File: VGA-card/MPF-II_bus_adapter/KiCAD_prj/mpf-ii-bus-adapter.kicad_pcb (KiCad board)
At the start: 2 copper layers, 100 x 34.4 mm, 33 parts, among them J1 Bus_Apple_II_Card_Side, J10 USER1_Sel, J11 INH_Sel, J12 RDY_Sel, J13 COLREF_Sel, J14 IOSTRB_Sel, J15 Q3_Sel, J16 Pin, J17 Pin, J18 Pin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

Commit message: PCB updated
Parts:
- moved J26 26.0 mm to (150.0, 103.2)
- moved J6 4.25 mm to (154.5, 100.7)
- moved J12 4.10 mm to (180.6, 100.7)
- moved J14 4.00 mm to (159.5, 103.2)
- moved J7 3.85 mm to (175.1, 100.7)
- moved J9 3.85 mm to (164.6, 100.7)
- moved J11 3.80 mm to (169.8, 100.7)
- moved J8 3.75 mm to (185.5, 100.7)
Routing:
- net GND: track 0.00 -> 114.4 mm
- net +5V: track 0.00 -> 87.4 mm
- net Net-(J3-Pin_1): track 0.00 -> 7.42 mm
- net Net-(J23-Pin_1): track 0.00 -> 3.71 mm
- net Net-(J24-Pin_1): track 0.00 -> 3.65 mm
- net Net-(J18-Pin_1): track 0.00 -> 3.52 mm
- net Net-(J17-Pin_1): track 0.00 -> 3.46 mm
- net Net-(J22-Pin_1): track 0.00 -> 3.33 mm
- net Net-(J25-Pin_1): track 0.00 -> 3.27 mm
- net Net-(J20-Pin_1): track 0.00 -> 3.24 mm
- net Net-(J16-Pin_1): track 0.00 -> 3.18 mm
- net Net-(J19-Pin_1): track 0.00 -> 3.14 mm
- net Net-(J21-Pin_1): track 0.00 -> 3.05 mm
- net /Q3: track 0.00 -> 0.91 mm
- net /A_PHI0: track 0.00 -> 0.83 mm
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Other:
- board size 100 x 34.4 mm -> 99.2 x 34.4 mm

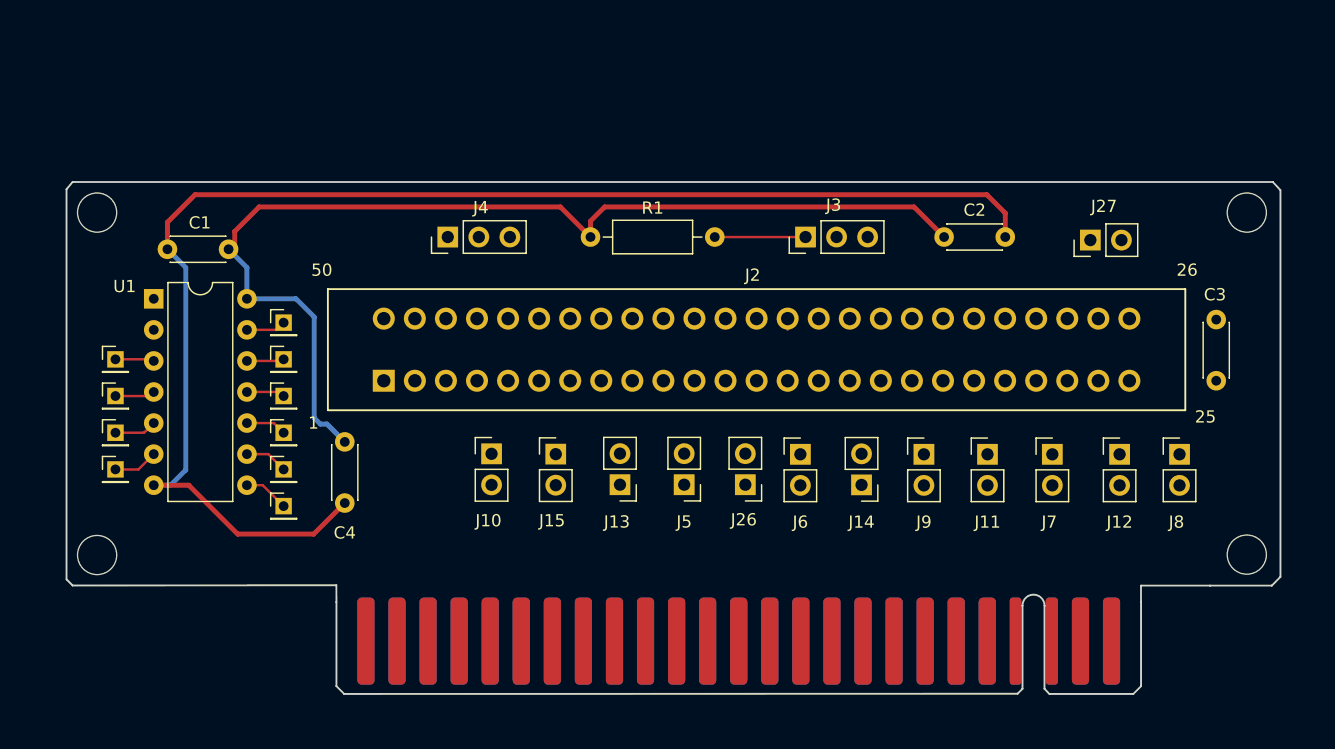
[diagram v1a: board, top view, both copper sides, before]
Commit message: PCB edge cut updated
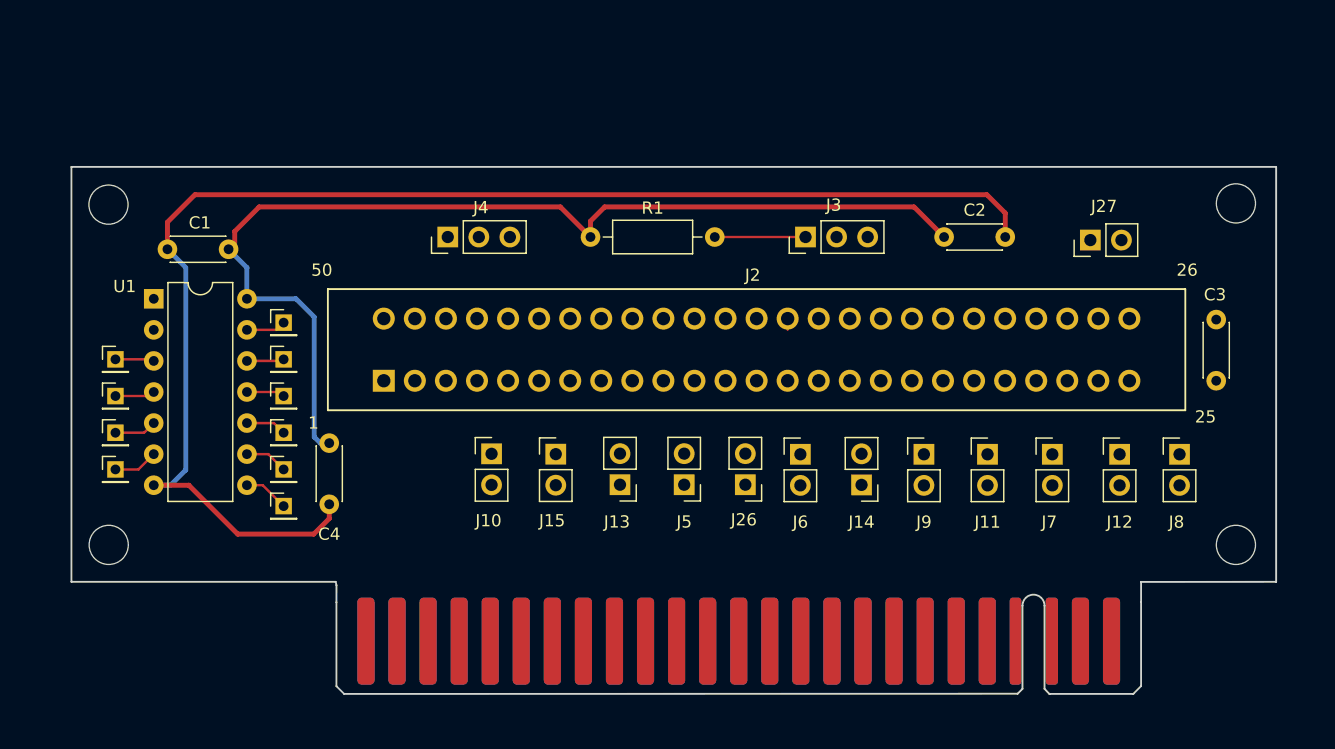
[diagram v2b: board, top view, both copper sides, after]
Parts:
- moved C4 1.27 mm to (116.0, 99.8)
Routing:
- net GND: track 114.4 -> 113.7 mm
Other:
- board size 99.2 x 34.4 mm -> 98.5 x 35.6 mm
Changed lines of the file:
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@@
 	(footprint "Capacitor_THT:C_Disc_D4.3mm_W1.9mm_P5.00mm"
 		(layer "F.Cu")
-		(at 117.25 99.71 -90)
+		(at 115.98 99.81 -90)
 		(descr "C, Disc series, Radial, pin pitch=5.00mm, , diameter*width=4.3*1.9mm^2, Capacitor, http://www.vishay.com/docs/45233/krseries.pdf")
 		(tags "C Disc series Radial pin pitch 5.00mm  diameter 4.3mm width 1.9mm Capacitor")
@@
 		)
 	)
-	(gr_circle
-		(center 97 80.96)
-		(end 98.25 81.96)
+	(gr_line
+		(start 193.4 77.225)
+		(end 193.4 111.15)
 		(stroke
-			(width 0.05)
+			(width 0.15)
 			(type default)
 		)
-		(fill none)
 		(layer "Edge.Cuts")
 	)
 	(gr_line
-		(start 193.05 111.46)
-		(end 188 111.46)
+		(start 94.9 77.225)
+		(end 193.4 77.225)
 		(stroke
 			(width 0.15)
@@
 	)
 	(gr_line
-		(start 193.05 111.46)
-		(end 193.75 110.745)
+		(start 116.5 111.15)
+		(end 94.9 111.15)
 		(stroke
 			(width 0.15)
@@
 		(layer "Edge.Cuts")
 	)
-	(gr_line
-		(start 193.75 110.75)
-		(end 193.75 79.125)
+	(gr_circle
+		(center 97.93 80.31)
+		(end 99.18 81.31)
 		(stroke
-			(width 0.15)
+			(width 0.05)
 			(type default)
 		)
+		(fill none)
 		(layer "Edge.Cuts")
 	)
 	(gr_line
-		(start 94.5 110.95)
-		(end 94.5 79.05)
+		(start 94.9 111.15)
+		(end 94.9 77.225)
 		(stroke
 			(width 0.15)
@@
 	)
 	(gr_line
-		(start 193.125 78.46)
-		(end 95 78.46)
+		(start 116.57 111.43)
+		(end 116.5 111.15)
 		(stroke
 			(width 0.15)
@@
 		(layer "Edge.Cuts")
 	)
-	(gr_line
-		(start 193.125002 78.454998)
-		(end 193.75 79.125)
+	(gr_circle
+		(center 97.95 108.13)
+		(end 96.7 109.13)
 		(stroke
-			(width 0.15)
+			(width 0.05)
 			(type default)
 		)
+		(fill none)
 		(layer "Edge.Cuts")
 	)
 	(gr_line
-		(start 95 78.46)
-		(end 94.5 79.05)
+		(start 193.4 111.15)
+		(end 182.35 111.16)
 		(stroke
 			(width 0.15)
@@
 	)
 	(gr_line
-		(start 95 111.45)
-		(end 94.5 110.95)
+		(start 182.353 112.825)
+		(end 182.35 111.16)
 		(stroke
 			(width 0.15)
@@
 	)
 	(gr_circle
-		(center 97 108.96)
-		(end 95.75 109.96)
+		(center 190.11 108.13)
+		(end 191.36 109.13)
 		(stroke
 			(width 0.05)
@@
 		(layer "Edge.Cuts")
 	)
-	(gr_line
-		(start 182.353 112.825)
-		(end 182.35 111.46)
-		(stroke
-			(width 0.15)
-			(type default)
-		)
-		(layer "Edge.Cuts")
-	)
 	(gr_circle
-		(center 191 108.925781)
-		(end 192.25 109.925781)
+		(center 190.11 80.21)
+		(end 191.36 79.21)
 		(stroke
 			(width 0.05)
@@
 	)
 	(gr_line
-		(start 116.56 111.43)
-		(end 95 111.45)
+		(start 116.567 112.825)
+		(end 116.57 111.43)
 		(stroke
 			(width 0.15)
@@
 		(layer "Edge.Cuts")
 	)
-	(gr_circle
-		(center 191 80.96)
-		(end 192.25 79.96)
+	(gr_rect
+		(start 94.9 77.225)
+		(end 193.4 111.15)
 		(stroke
-			(width 0.05)
+			(width 0.2)
 			(type default)
 		)
 		(fill none)
-		(layer "Edge.Cuts")
+		(layer "Margin")
 	)
 	(gr_line
-		(start 116.567 112.825)
-		(end 116.559988 111.43)
+		(start 116.61 111.44)
+		(end 116.43 111.16)
 		(stroke
-			(width 0.15)
-			(type default)
-		)
-		(layer "Edge.Cuts")
-	)
-	(gr_line
-		(start 188 111.46)
-		(end 182.35 111.46)
-		(stroke
-			(width 0.15)
+			(width 0.1)
 			(type default)
 		)
-		(layer "Edge.Cuts")
+		(layer "Margin")
 	)
 	(segment
@@
 	)
 	(segment
-		(start 114.75 97.75)
-		(end 115.25 98.25)
+		(start 114.75 99.31)
+		(end 115.25 99.81)
 		(width 0.4)
 		(layer "B.Cu")
@@
 	)
 	(segment
-		(start 115.25 98.25)
-		(end 115.79 98.25)
+		(start 115.25 99.81)
+		(end 115.98 99.81)
 		(width 0.4)
 		(layer "B.Cu")
@@
 	)
 	(segment
-		(start 109.25 85.46)
-		(end 107.75 83.96)
-		(width 0.4)
-		(layer "B.Cu")
-		(net 1)
-	)
-	(segment
 		(start 114.75 89.5)
-		(end 114.75 97.75)
+		(end 114.75 99.31)
 		(width 0.4)
 		(layer "B.Cu")
@@
 	)
 	(segment
-		(start 115.79 98.25)
-		(end 117.25 99.71)
+		(start 109.25 85.46)
+		(end 107.75 83.96)
 		(width 0.4)
 		(layer "B.Cu")
@@
 	)
 	(segment
+		(start 115.98 105.98)
+		(end 115.98 104.81)
+		(width 0.4)
+		(layer "F.Cu")
+		(net 2)
+	)
+	(segment
 		(start 171.25 81)
 		(end 171.25 82.96)
@@
 	)
 	(segment
-		(start 117.25 104.71)
-		(end 114.71 107.25)
+		(start 105 79.5)
+		(end 169.75 79.5)
 		(width 0.4)
 		(layer "F.Cu")
@@
 	)
 	(segment
-		(start 105 79.5)
-		(end 169.75 79.5)
+		(start 114.71 107.25)
+		(end 115.98 105.98)
 		(width 0.4)
 		(layer "F.Cu")

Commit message: PCB updated
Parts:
- added G***: LOGO, LOGO, F.Cu at (103.9, 107.7)
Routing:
- net /PHI1: track 0.00 -> 87.8 mm, vias 0 -> 1
- net +5V: track 87.1 -> 153.1 mm
- net /M_DEVSEL: track 0.00 -> 54.5 mm, vias 0 -> 2
- net /M_PHI2: track 0.00 -> 43.6 mm
- net Net-(J4-Pin_1): track 0.00 -> 35.2 mm
- net /D3: track 0.00 -> 31.2 mm
- net /D2: track 0.00 -> 30.1 mm
- net -5V: track 0.00 -> 29.8 mm
- net /2M: track 0.00 -> 29.1 mm, vias 0 -> 2
- net +12V: track 0.00 -> 28.9 mm
- net /D1: track 0.00 -> 28.8 mm
- net /D7: track 0.00 -> 28.7 mm
- net /D0: track 0.00 -> 28.3 mm
- net /D5: track 0.80 -> 28.9 mm
- net /EXT6: track 0.00 -> 28.0 mm, vias 0 -> 1
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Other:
- board text added: "MPF-II Bus Adapter, Rev A"

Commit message: PCB is ready
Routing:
- net GND: track 140.2 -> 173.7 mm
- net /RESET: track 0.00 -> 32.5 mm
- net /INTIN: track 0.00 -> 28.5 mm
- net /DMAIN: track 0.00 -> 27.4 mm
- net /M_IRQ: track 0.00 -> 25.4 mm, vias 0 -> 1
- net /A_IRQ: track 0.00 -> 24.9 mm
- net /M_RDY: track 0.00 -> 23.0 mm
- net /INTOUT: track 0.00 -> 22.9 mm, vias 0 -> 1
- net /DMAOUT: track 0.00 -> 21.9 mm, vias 0 -> 1
- net /EXTE: track 0.62 -> 18.3 mm, vias 0 -> 1
- net /A_NMI: track 0.00 -> 16.6 mm
- net /M_DMA: track 0.00 -> 16.3 mm
- net /M_NMI: track 0.00 -> 15.7 mm
- net /M_INH: track 0.00 -> 15.7 mm, vias 0 -> 1
- net /A_RDY: track 0.00 -> 14.2 mm
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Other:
- board text added: "mpf-ii_retro_6502 at Github"

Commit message: PCB updated
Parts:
- moved G*** 0.75 mm to (104.6, 107.6)
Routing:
- net +5V: track 153.1 -> 152.0 mm
- net GND: track 173.7 -> 172.5 mm
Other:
- outline, holes or cut-outs redrawn
- board text added: "mpf-ii_retro_6502 on GitHub"
- board text removed: "mpf-ii_retro_6502 at Github"
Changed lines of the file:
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@@
 	(footprint "LOGO"
 		(layer "F.Cu")
-		(at 103.9 107.725)
+		(at 104.648751 107.644678)
 		(property "Reference" "G***"
 			(at 0 0 0)
@@
 	)
 	(gr_circle
-		(center 97.93 80.31)
-		(end 99.18 81.31)
+		(center 98.09 80.320781)
+		(end 99.34 81.320781)
 		(stroke
 			(width 0.05)
@@
 	)
 	(gr_circle
-		(center 97.95 108.13)
-		(end 96.7 109.13)
+		(center 98.1 107.390781)
+		(end 96.85 108.390781)
 		(stroke
 			(width 0.05)
@@
 	)
 	(gr_circle
-		(center 190.11 108.13)
-		(end 191.36 109.13)
+		(center 190.225 107.425)
+		(end 191.475 108.425)
 		(stroke
 			(width 0.05)
@@
 	)
 	(gr_circle
-		(center 190.11 80.21)
-		(end 191.36 79.21)
+		(center 190.47 80.320781)
+		(end 191.72 79.320781)
 		(stroke
 			(width 0.05)
@@
 		(layer "Margin")
 	)
-	(gr_text "mpf-ii_retro_6502 at Github"
-		(at 164.15 78.75 0)
+	(gr_text "mpf-ii_retro_6502 on GitHub"
+		(at 159.42 78.77 0)
 		(layer "F.SilkS")
 		(effects
@@
 	)
 	(segment
-		(start 188.5 97.85)
-		(end 189.5 98.85)
-		(width 0.5)
-		(layer "F.Cu")
-		(net 1)
-	)
-	(segment
 		(start 108.25 82.5)
 		(end 108.25 83.46)
@@
 	)
 	(segment
-		(start 179.94 110.61)
-		(end 179.94 116)
+		(start 187.95 104.575)
+		(end 187.95 98.4)
 		(width 0.5)
 		(layer "F.Cu")
@@
 	)
 	(segment
-		(start 181.2 109.35)
+		(start 179.94 116)
 		(end 179.94 110.61)
 		(width 0.5)
@@
 	)
 	(segment
-		(start 189.5 98.85)
-		(end 189.5 104.05)
+		(start 186.2 105.25)
+		(end 187.275 105.25)
 		(width 0.5)
 		(layer "F.Cu")
@@
 	)
 	(segment
-		(start 184.2 109.35)
-		(end 181.2 109.35)
+		(start 179.975 86.75)
+		(end 182.625 86.75)
 		(width 0.5)
 		(layer "F.Cu")
@@
 	)
 	(segment
-		(start 179.975 86.75)
-		(end 182.625 86.75)
+		(start 187.95 98.4)
+		(end 188.5 97.85)
 		(width 0.5)
 		(layer "F.Cu")
@@
 	)
 	(segment
+		(start 183.25 106.85)
+		(end 184.6 106.85)
+		(width 0.5)
+		(layer "F.Cu")
+		(net 1)
+	)
+	(segment
 		(start 137.34 81.66)
 		(end 137.34 82.96)
@@
 	)
 	(segment
-		(start 188.5 94.71)
-		(end 188.5 97.85)
+		(start 184.6 106.85)
+		(end 186.2 105.25)
 		(width 0.5)
 		(layer "F.Cu")
@@
 	)
 	(segment
-		(start 184.15 88.275)
-		(end 184.15 91.96)
+		(start 187.275 105.25)
+		(end 187.95 104.575)
 		(width 0.5)
 		(layer "F.Cu")
@@
 	)
 	(segment
-		(start 189.5 104.05)
-		(end 184.2 109.35)
+		(start 188.5 97.85)
+		(end 188.5 94.71)
+		(width 0.5)
+		(layer "F.Cu")
+		(net 1)
+	)
+	(segment
+		(start 179.94 110.61)
+		(end 183.25 107.3)
+		(width 0.5)
+		(layer "F.Cu")
+		(net 1)
+	)
+	(segment
+		(start 184.15 88.275)
+		(end 184.15 91.96)
 		(width 0.5)
 		(layer "F.Cu")
@@
 	)
 	(segment
+		(start 183.25 107.3)
+		(end 183.25 106.85)
+		(width 0.5)
+		(layer "F.Cu")
+		(net 1)
+	)
+	(segment
 		(start 108.25 83.46)
 		(end 107.75 83.96)
@@
 	)
 	(segment
+		(start 188.8 104.85)
+		(end 187.575 106.075)
+		(width 0.2)
+		(layer "B.Cu")
+		(net 2)
+	)
+	(segment
 		(start 102.75 83.96)
 		(end 104.25 85.46)
@@
 	)
 	(segment
+		(start 190.125 91.335)
+		(end 190.125 96.4)
+		(width 0.2)
+		(layer "B.Cu")
+		(net 2)
+	)
+	(segment
 		(start 181.45 86.25)
 		(end 181.4 86.3)
@@
 	)
 	(segment
-		(start 190.64 91.85)
-		(end 190.65 91.85)
+		(start 185.15 107.625)
+		(end 184.025 107.625)
 		(width 0.2)
 		(layer "B.Cu")
@@
 	)
 	(segment
-		(start 190.65 91.85)
-		(end 190.65 104.1)
-		(width 0.2)
-		(layer "B.Cu")
-		(net 2)
-	)
-	(segment
-		(start 188.5 89.71)
-		(end 190.64 91.85)
+		(start 184.025 107.625)
+		(end 184.025 107.775)
 		(width 0.2)
 		(layer "B.Cu")
@@
 	)
 	(segment
-		(start 179.94 111.86)
-		(end 179.94 116)
+		(start 186.7 106.075)
+		(end 185.15 107.625)
 		(width 0.2)
 		(layer "B.Cu")
@@
 	)
 	(segment
+		(start 188.8 100.325)
+		(end 188.8 104.85)
+		(width 0.2)
+		(layer "B.Cu")
+		(net 2)
+	)
+	(segment
 		(start 180.75 84.85)
 		(end 180.75 83.21)
@@
 	)
 	(segment
-		(start 181.625 110.175)
+		(start 179.94 111.86)
+		(end 179.94 116)
+		(width 0.2)
+		(layer "B.Cu")
+		(net 2)
+	)
+	(segment
+		(start 184.025 107.775)
 		(end 179.94 111.86)
 		(width 0.2)
@@
 	)
 	(segment
-		(start 190.725 104.175)
-		(end 184.725 110.175)
+		(start 189.475 99.65)
+		(end 188.8 100.325)
+		(width 0.2)
+		(layer "B.Cu")
+		(net 2)
+	)
+	(segment
+		(start 190.125 96.4)
+		(end 189.475 97.05)
 		(width 0.2)
 		(layer "B.Cu")
@@
 	)
 	(segment
-		(start 184.725 110.175)
-		(end 181.625 110.175)
+		(start 189.475 97.05)
+		(end 189.475 99.65)
+		(width 0.2)
+		(layer "B.Cu")
+		(net 2)
+	)
+	(segment
+		(start 188.5 89.71)
+		(end 190.125 91.335)
 		(width 0.2)
 		(layer "B.Cu")
@@
 	)
 	(segment
-		(start 190.65 104.1)
-		(end 190.725 104.175)
-		(width 0.2)
+		(start 103 103.25)
+		(end 101.63 103.25)
+		(width 0.4)
 		(layer "B.Cu")
 		(net 2)
 	)
 	(segment
-		(start 103 103.25)
-		(end 101.63 103.25)
-		(width 0.4)
+		(start 187.575 106.075)
+		(end 186.7 106.075)
+		(width 0.2)
 		(layer "B.Cu")
 		(net 2)

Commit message: Filled zones added
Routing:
- added copper zone on B.Cu, net GND
- added copper zone on F.Cu, net GND
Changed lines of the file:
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@@
 		(net 76)
 	)
+	(zone
+		(net 2)
+		(net_name "GND")
+		(layer "F.Cu")
+		(hatch edge 0.5)
+		(connect_pads
+			(clearance 0.5)
+		)
+		(min_thickness 0.25)
+		(filled_areas_thickness no)
+		(fill yes
+			(thermal_gap 0.5)
+			(thermal_bridge_width 0.5)
+		)
+		(polygon
+			(pts
+				(xy 91.4 76.13) (xy 195.46 76.34) (xy 195.82 122.54) (xy 91.54 122.05) (xy 91.41 76.13) (xy 91.42 76.14)
+			)
+		)
+	)
+	(zone
+		(net 2)
+		(net_name "GND")
+		(layer "B.Cu")
+		(hatch edge 0.5)
+		(priority 1)
+		(connect_pads
+			(clearance 0.5)
+		)
+		(min_thickness 0.25)
+		(filled_areas_thickness no)
+		(fill yes
+			(thermal_gap 0.5)
+			(thermal_bridge_width 0.5)
+		)
+		(polygon
+			(pts
+				(xy 91.49 75.63) (xy 195.7 75.92) (xy 196.2 122.83) (xy 91.06 122.34) (xy 91.5 75.62) (xy 91.5 75.65)
+				(xy 91.5 75.62)
+			)
+		)
+	)
 )

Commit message: Schematics updated with bus pinheader connector
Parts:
- added J28: Conn_02x25_Counter_Clockwise, Connector_PinHeader_2.54mm:PinHeader_2x25_P2.54mm_Vertical, F.Cu at (118.8, 69.5)

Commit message: PCB updated
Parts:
- J28: value Conn_02x25_Counter_Clockwise -> MPF-Bus
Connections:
- net /A_INH renamed /INH
- J1 pad 32: /M_INH -> /EXTM
- J1 pad 33: Net-(J1--12V) -> unconnected-(J1--12V-Pad33)
- J1 pad 39: /M_USER1 -> /IODIS
- J1 pad 40: /M_PHI2 -> /PHI2
- J10 pad 2: /M_USER1 -> /IODIS
- J11 pad 2: /M_INH -> /EXTM
- J2 pad 33: -12V -> unconnected-(J2--12V-Pad33)
- J28 pad 1: unconnected-(J28-Pin_1-Pad1) -> /IOSEL
- J28 pad 10: unconnected-(J28-Pin_10-Pad10) -> /A8
- J28 pad 11: unconnected-(J28-Pin_11-Pad11) -> /A9
- J28 pad 12: unconnected-(J28-Pin_12-Pad12) -> /A10
- J28 pad 13: unconnected-(J28-Pin_13-Pad13) -> /A11
- J28 pad 14: unconnected-(J28-Pin_14-Pad14) -> /A12
- J28 pad 15: unconnected-(J28-Pin_15-Pad15) -> /A13
- J28 pad 16: unconnected-(J28-Pin_16-Pad16) -> /A14
- J28 pad 17: unconnected-(J28-Pin_17-Pad17) -> /A15
- J28 pad 18: unconnected-(J28-Pin_18-Pad18) -> /RW
- J28 pad 19: unconnected-(J28-Pin_19-Pad19) -> /EXT8
- J28 pad 2: unconnected-(J28-Pin_2-Pad2) -> /A0
- J28 pad 20: unconnected-(J28-Pin_20-Pad20) -> /EXTE
- J28 pad 21: unconnected-(J28-Pin_21-Pad21) -> /M_RDY
- J28 pad 22: unconnected-(J28-Pin_22-Pad22) -> /M_DMA
- J28 pad 23: unconnected-(J28-Pin_23-Pad23) -> /INTOUT
- J28 pad 24: unconnected-(J28-Pin_24-Pad24) -> /DMAOUT
- J28 pad 25: unconnected-(J28-Pin_25-Pad25) -> +5V
- J28 pad 26: unconnected-(J28-Pin_26-Pad26) -> GND
- J28 pad 27: unconnected-(J28-Pin_27-Pad27) -> /DMAIN
- J28 pad 28: unconnected-(J28-Pin_28-Pad28) -> /INTIN
- J28 pad 29: unconnected-(J28-Pin_29-Pad29) -> /M_NMI
- J28 pad 3: unconnected-(J28-Pin_3-Pad3) -> /A1
- J28 pad 30: unconnected-(J28-Pin_30-Pad30) -> /M_IRQ
- J28 pad 31: unconnected-(J28-Pin_31-Pad31) -> /RESET
- J28 pad 32: unconnected-(J28-Pin_32-Pad32) -> /EXTM
- J28 pad 34: unconnected-(J28-Pin_34-Pad34) -> -5V
- J28 pad 35: unconnected-(J28-Pin_35-Pad35) -> /EXT6
- J28 pad 36: unconnected-(J28-Pin_36-Pad36) -> /SOUND_IN
- J28 pad 37: unconnected-(J28-Pin_37-Pad37) -> /2M
- J28 pad 38: unconnected-(J28-Pin_38-Pad38) -> /PHI1
- J28 pad 39: unconnected-(J28-Pin_39-Pad39) -> /IODIS
- J28 pad 4: unconnected-(J28-Pin_4-Pad4) -> /A2
- J28 pad 40: unconnected-(J28-Pin_40-Pad40) -> /PHI2
- J28 pad 41: unconnected-(J28-Pin_41-Pad41) -> /M_DEVSEL
- J28 pad 42: unconnected-(J28-Pin_42-Pad42) -> /D7
- J28 pad 43: unconnected-(J28-Pin_43-Pad43) -> /D6
- J28 pad 44: unconnected-(J28-Pin_44-Pad44) -> /D5
- J28 pad 45: unconnected-(J28-Pin_45-Pad45) -> /D4
- J28 pad 46: unconnected-(J28-Pin_46-Pad46) -> /D3
- J28 pad 47: unconnected-(J28-Pin_47-Pad47) -> /D2
- J28 pad 48: unconnected-(J28-Pin_48-Pad48) -> /D1
- J28 pad 49: unconnected-(J28-Pin_49-Pad49) -> /D0
- J28 pad 5: unconnected-(J28-Pin_5-Pad5) -> /A3
- J28 pad 50: unconnected-(J28-Pin_50-Pad50) -> +12V
- J28 pad 6: unconnected-(J28-Pin_6-Pad6) -> /A4
- J28 pad 7: unconnected-(J28-Pin_7-Pad7) -> /A5
- J28 pad 8: unconnected-(J28-Pin_8-Pad8) -> /A6
- J28 pad 9: unconnected-(J28-Pin_9-Pad9) -> /A7
- J4 pad 3: /M_PHI2 -> /PHI2
- R1 pad 1: +5V -> Net-(J3-Pin_1)
- R1 pad 2: Net-(J3-Pin_1) -> +5V
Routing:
- net /PHI2: track 0.00 -> 43.6 mm
- net /M_PHI2: track 43.6 -> 0.00 mm
- net /M_USER1: track 27.9 -> 0.00 mm, vias 1 -> 0
- net /IODIS: track 0.00 -> 27.9 mm, vias 0 -> 1
- net /M_INH: track 15.7 -> 0.00 mm, vias 1 -> 0
- net /EXTM: track 0.00 -> 15.7 mm, vias 0 -> 1
